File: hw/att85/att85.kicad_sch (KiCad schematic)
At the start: 45 parts, among them J101 Barrel_Jack_Switch, J102 Screw_Terminal_01x03, J103 AVR-ISP-6, J104 Conn_01x02, J105 Conn_01x02, Q101 BC817, SW101 SW_Push, SW102 SW_Push, SW103 SW_Push, SW104 SW_Push, SW105 SW_Push, SW106 SW_Push, U101 ATtiny85-20P, U102 MT3608-MODULE, U105 74AHC1G125

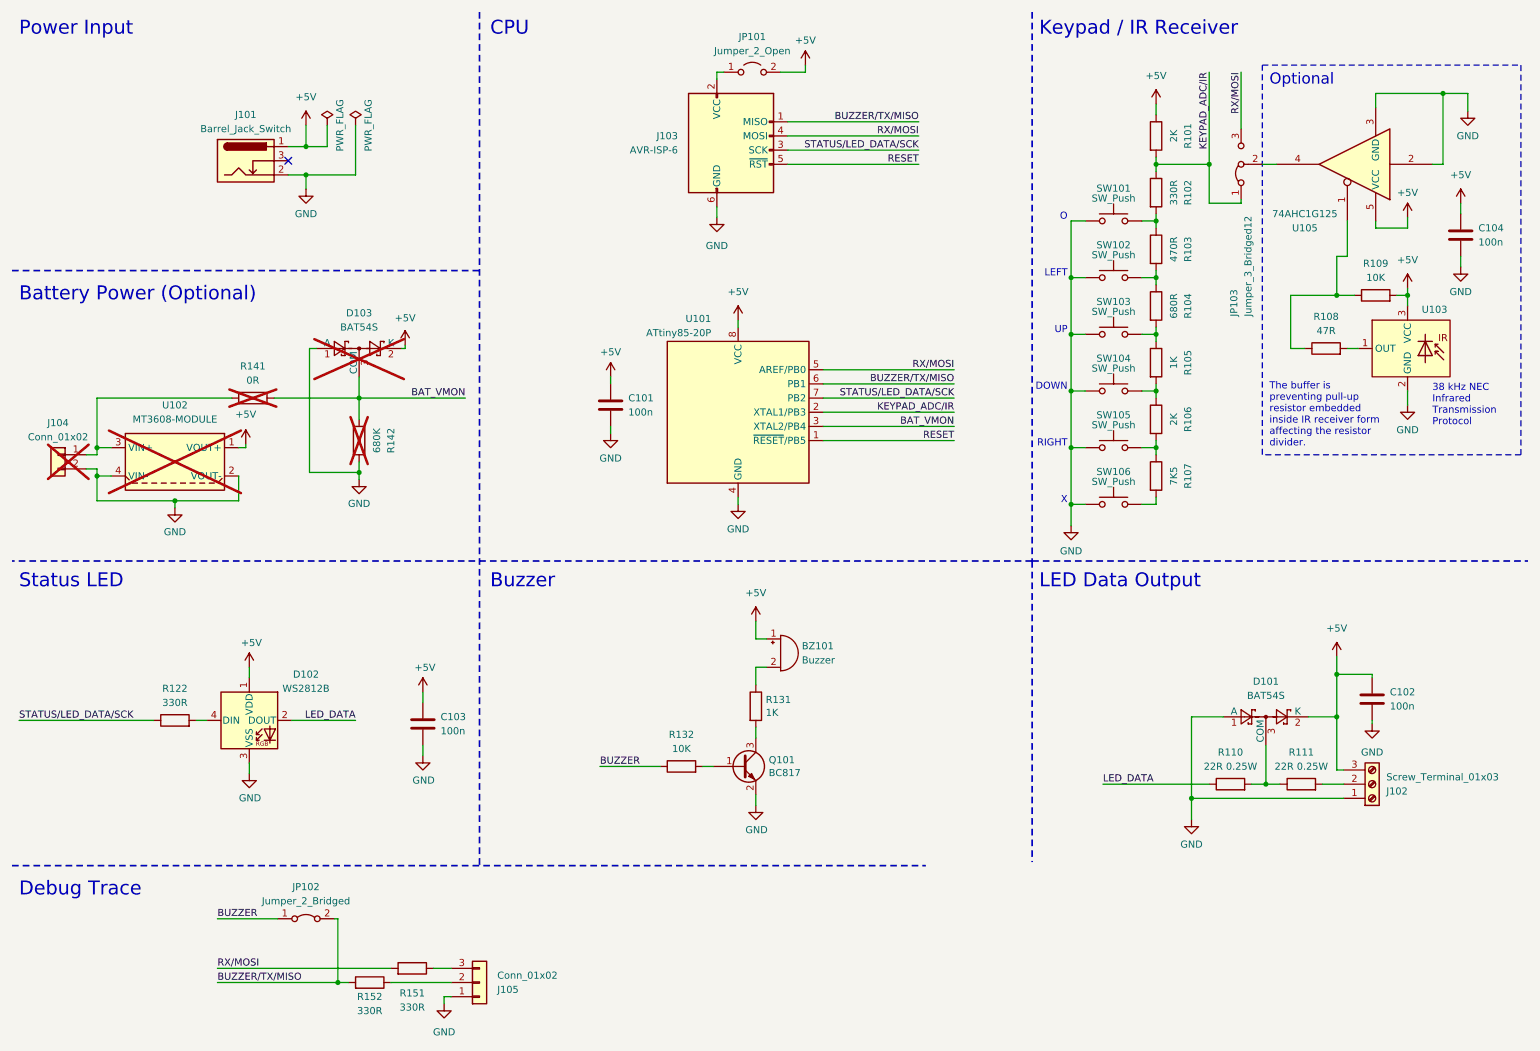
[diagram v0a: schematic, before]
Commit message: feat(hw): remove unused components, wire IR to separate uC pin
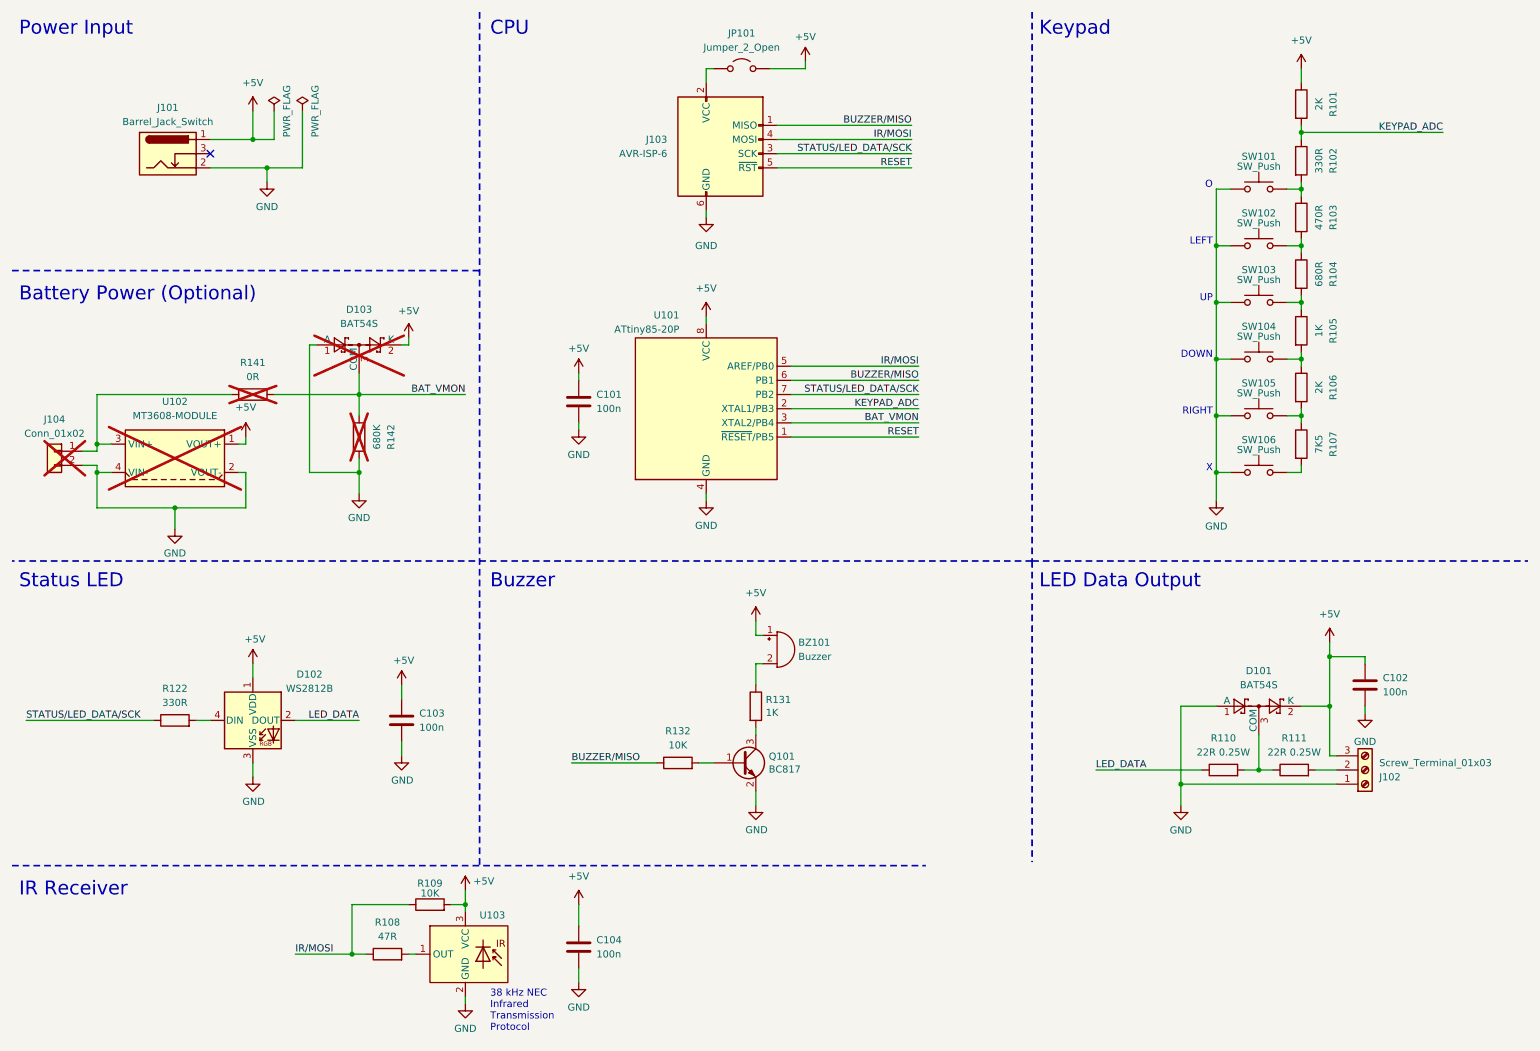
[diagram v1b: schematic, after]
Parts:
- removed J105: Conn_01x02, Connector_PinHeader_2.54mm:PinHeader_1x03_P2.54mm_Vertical, symbol Connector_Generic:Conn_01x03
- removed JP102: Jumper_2_Bridged, Jumper:SolderJumper-2_P1.3mm_Bridged_RoundedPad1.0x1.5mm, symbol Jumper:Jumper_2_Bridged
- removed JP103: Jumper_3_Bridged12, Jumper:SolderJumper-3_P1.3mm_Bridged12_RoundedPad1.0x1.5mm, symbol Jumper:Jumper_3_Bridged12
- removed R151, R152: 330R, Resistor_SMD:R_0805_2012Metric_Pad1.20x1.40mm_HandSolder, symbol Device:R
- removed U105: 74AHC1G125, Package_TO_SOT_SMD:SOT-23-5_HandSoldering, symbol 74xGxx:74AHC1G125
- U101: footprint Package_DIP:DIP-8_W7.62mm_Socket -> Package_DIP:DIP-8_W7.62mm
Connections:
- net BUZZER/TX/MISO is gone; now on net BUZZER/MISO: J103.1 (MISO), U101.6 (PB1)
- net RX/MOSI is gone; now on net IR/MOSI: J103.4 (MOSI), U101.5 (AREF/PB0)
- net IR/MOSI: now reaches R108.1, R109.1
- net BUZZER renamed BUZZER/MISO
- net KEYPAD_ADC/IR renamed KEYPAD_ADC
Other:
- note added: "IR Receiver"
- note added: "Keypad"
- note removed: "Debug Trace"
- note removed: "Keypad / IR Receiver"
- note removed: "Optional"
- note removed: "The buffer is preventing pull-up resistor embedded inside IR receiver form affecting the resistor divider."
- moved on the sheet: BZ101, C101, C102, C103, C104, D101, D102, D103, J101, J102, J103, J104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

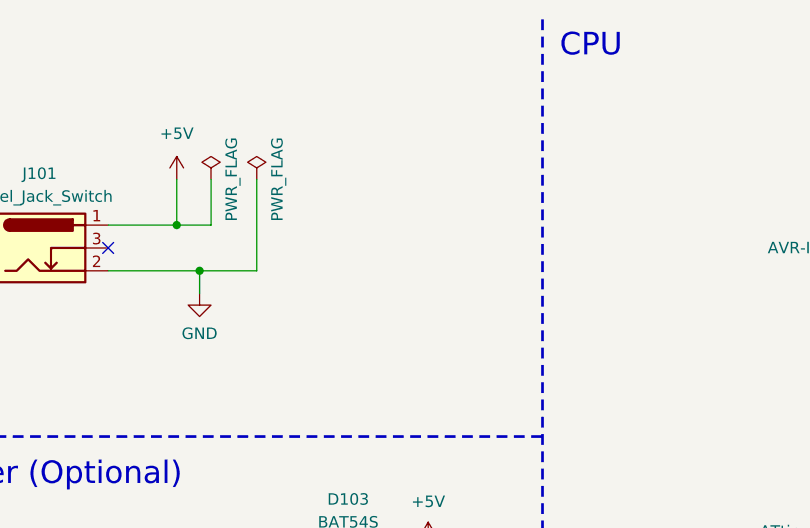
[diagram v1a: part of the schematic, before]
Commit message: feat(hw): improve layout and add a mounting hole
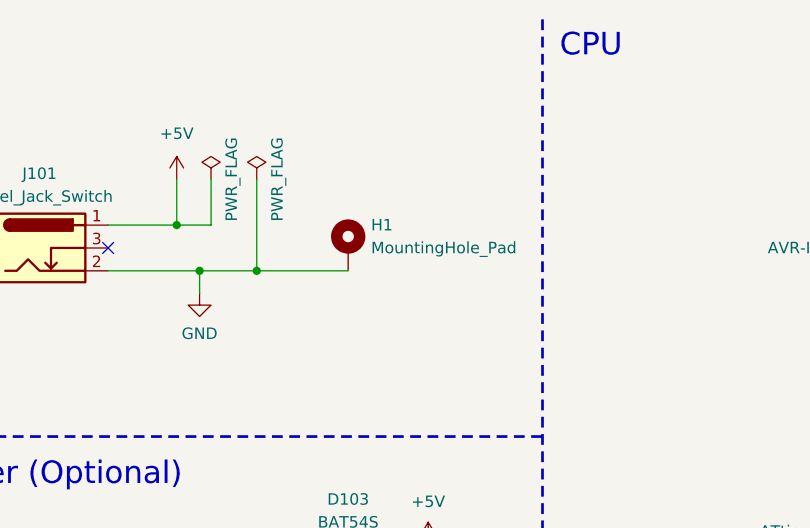
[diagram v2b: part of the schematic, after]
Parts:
- added H1: MountingHole_Pad, MountingHole:MountingHole_2.5mm_Pad_TopBottom, symbol Mechanical:MountingHole_Pad
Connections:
- net GND: now also H1.1
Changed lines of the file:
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@@
 	)
 	(junction
+		(at 64.77 40.64)
+		(diameter 0)
+		(color 0 0 0 0)
+	)
+	(junction
 		(at 243.84 74.93)
 		(diameter 0)
@@
 	(wire
 		(pts
+			(xy 64.77 40.64) (xy 74.93 40.64)
+		)
+		(stroke
+			(width 0)
+			(type default)
+		)
+	)
+	(wire
+		(pts
 			(xy 138.43 22.86) (xy 137.16 22.86)
 		)
@@
 					(unit 1)
 				)
+			)
+		)
+	)
+	(symbol
+		(lib_id "Mechanical:MountingHole_Pad")
+		(at 74.93 38.1 0)
+		(unit 1)
+		(exclude_from_sim yes)
+		(in_bom no)
+		(on_board yes)
+		(dnp no)
+		(fields_autoplaced yes)
+		(property "Reference" "H1"
+			(at 77.47 35.5599 0)
+			(effects
+				(font
+					(size 1.27 1.27)
+				)
+				(justify left)
+			)
+		)
+		(property "Value" "MountingHole_Pad"
+			(at 77.47 38.0999 0)
+			(effects
+				(font
+					(size 1.27 1.27)
+				)
+				(justify left)
+			)
+		)
+		(property "Footprint" "MountingHole:MountingHole_2.5mm_Pad_TopBottom"
+			(at 74.93 38.1 0)
+			(effects
+				(font
+					(size 1.27 1.27)
+				)
+				(hide yes)
+			)
+		)
+		(property "Datasheet" "~"
+			(at 74.93 38.1 0)
+			(effects
+				(font
+					(size 1.27 1.27)
+				)
+				(hide yes)
+			)
+		)
+		(property "Description" "Mounting Hole with connection"
+			(at 74.93 38.1 0)
+			(effects
+				(font
+					(size 1.27 1.27)
+				)
+				(hide yes)
+			)
+		)
+		(pin "1"
+		)
+		(instances
+			(project "att85"
+				(path "/fc4ba96f-a9f8-4f1a-a9c5-2b16679a6770"
+					(reference "H1")
+					(unit 1)
+				)

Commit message: fix(hw): minor improvements
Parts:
- added C105: 10u, Capacitor_SMD:C_1206_3216Metric_Pad1.33x1.80mm_HandSolder, symbol Device:C
- R109: value 10K -> 20K; now not fitted
- U103: value ~ -> VS1838B
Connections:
- net +5V: now also C105.1
- net GND: now also C105.2
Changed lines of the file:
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@@
 	)
 	(junction
+		(at 114.3 186.69)
+		(diameter 0)
+		(color 0 0 0 0)
+	)
+	(junction
 		(at 64.77 40.64)
 		(diameter 0)
@@
 	)
 	(junction
+		(at 114.3 173.99)
+		(diameter 0)
+		(color 0 0 0 0)
+	)
+	(junction
 		(at 228.6 85.09)
 		(diameter 0)
@@
 	(wire
 		(pts
+			(xy 114.3 186.69) (xy 114.3 184.15)
+		)
+		(stroke
+			(width 0)
+			(type default)
+		)
+	)
+	(wire
+		(pts
 			(xy 233.68 148.59) (xy 236.22 148.59)
 		)
@@
 	(wire
 		(pts
-			(xy 114.3 172.72) (xy 114.3 176.53)
+			(xy 114.3 172.72) (xy 114.3 173.99)
 		)
 		(stroke
@@
 	(wire
 		(pts
+			(xy 127 173.99) (xy 127 176.53)
+		)
+		(stroke
+			(width 0)
+			(type default)
+		)
+	)
+	(wire
+		(pts
 			(xy 83.82 71.12) (xy 83.82 72.39)
 		)
@@
 	(wire
 		(pts
-			(xy 114.3 186.69) (xy 114.3 184.15)
+			(xy 114.3 173.99) (xy 114.3 176.53)
+		)
+		(stroke
+			(width 0)
+			(type default)
+		)
+	)
+	(wire
+		(pts
+			(xy 114.3 187.96) (xy 114.3 186.69)
 		)
 		(stroke
@@
 	(wire
 		(pts
+			(xy 114.3 173.99) (xy 127 173.99)
+		)
+		(stroke
+			(width 0)
+			(type default)
+		)
+	)
+	(wire
+		(pts
 			(xy 255.27 138.43) (xy 255.27 137.16)
 		)
@@
 	(wire
 		(pts
+			(xy 114.3 186.69) (xy 127 186.69)
+		)
+		(stroke
+			(width 0)
+			(type default)
+		)
+	)
+	(wire
+		(pts
 			(xy 93.98 170.18) (xy 93.98 172.72)
 		)
@@
 	(wire
 		(pts
+			(xy 127 186.69) (xy 127 184.15)
+		)
+		(stroke
+			(width 0)
+			(type default)
+		)
+	)
+	(wire
+		(pts
 			(xy 73.66 172.72) (xy 73.66 181.61)
 		)
@@
 	(symbol
 		(lib_id "power:GND")
-		(at 114.3 186.69 0)
+		(at 114.3 187.96 0)
 		(unit 1)
 		(exclude_from_sim no)
@@
 		(fields_autoplaced yes)
 		(property "Reference" "#PWR0130"
-			(at 114.3 193.04 0)
+			(at 114.3 194.31 0)
 			(effects
 				(font
@@
 		)
 		(property "Value" "GND"
-			(at 114.3 191.135 0)
+			(at 114.3 192.405 0)
 			(effects
 				(font
@@
 		)
 		(property "Footprint" ""
-			(at 114.3 186.69 0)
+			(at 114.3 187.96 0)
 			(effects
 				(font
@@
 		)
 		(property "Datasheet" ""
-			(at 114.3 186.69 0)
+			(at 114.3 187.96 0)
 			(effects
 				(font
@@
 		)
 		(property "Description" "Power symbol creates a global label with name \"GND\" , ground"
-			(at 114.3 186.69 0)
+			(at 114.3 187.96 0)
 			(effects
 				(font
@@
 	)
 	(symbol
+		(lib_id "Device:C")
+		(at 127 180.34 0)
+		(unit 1)
+		(exclude_from_sim no)
+		(in_bom yes)
+		(on_board yes)
+		(dnp no)
+		(fields_autoplaced yes)
+		(property "Reference" "C105"
+			(at 130.175 179.07 0)
+			(effects
+				(font
+					(size 1.27 1.27)
+				)
+				(justify left)
+			)
+		)
+		(property "Value" "10u"
+			(at 130.175 181.61 0)
+			(effects
+				(font
+					(size 1.27 1.27)
+				)
+				(justify left)
+			)
+		)
+		(property "Footprint" "Capacitor_SMD:C_1206_3216Metric_Pad1.33x1.80mm_HandSolder"
+			(at 127.9652 184.15 0)
+			(effects
+				(font
+					(size 1.27 1.27)
+				)
+				(hide yes)
+			)
+		)
+		(property "Datasheet" "~"
+			(at 127 180.34 0)
+			(effects
+				(font
+					(size 1.27 1.27)
+				)
+				(hide yes)
+			)
+		)
+		(property "Description" "Unpolarized capacitor"
+			(at 127 180.34 0)
+			(effects
+				(font
+					(size 1.27 1.27)
+				)
+				(hide yes)
+			)
+		)
+		(pin "2"
+		)
+		(pin "1"
+		)
+		(instances
+			(project "att85"
+				(path "/fc4ba96f-a9f8-4f1a-a9c5-2b16679a6770"
+					(reference "C105")
+					(unit 1)
+				)
+			)
+		)
+	)
+	(symbol
 		(lib_id "Device:R")
 		(at 87.63 172.72 90)
@@
 		(in_bom yes)
 		(on_board yes)
-		(dnp no)
+		(dnp yes)
 		(property "Reference" "R109"
 			(at 87.63 168.91 90)
@@
 			)
 		)
-		(property "Value" "10K"
+		(property "Value" "20K"
 			(at 87.63 170.688 90)
 			(effects
@@
 		(dnp no)
 		(property "Reference" "U103"
-			(at 96.52 174.625 0)
+			(at 96.266 173.228 0)
 			(effects
 				(font
@@
 			)
 		)
-		(property "Value" "~"
-			(at 92.71 181.61 0)
+		(property "Value" "VS1838B"
+			(at 100.584 175.26 0)
 			(effects
 				(font

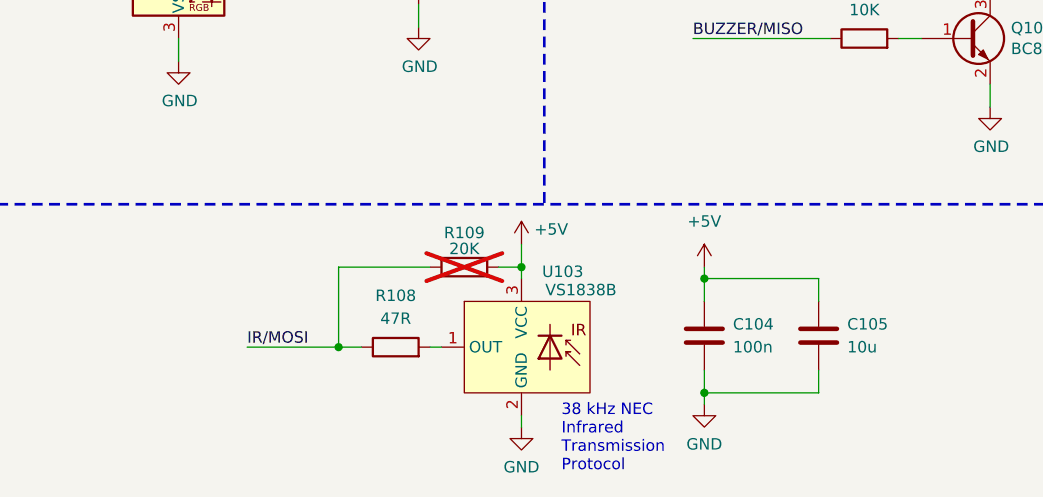
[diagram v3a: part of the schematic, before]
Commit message: fix(hw): move IR receiver resistor according the datasheet
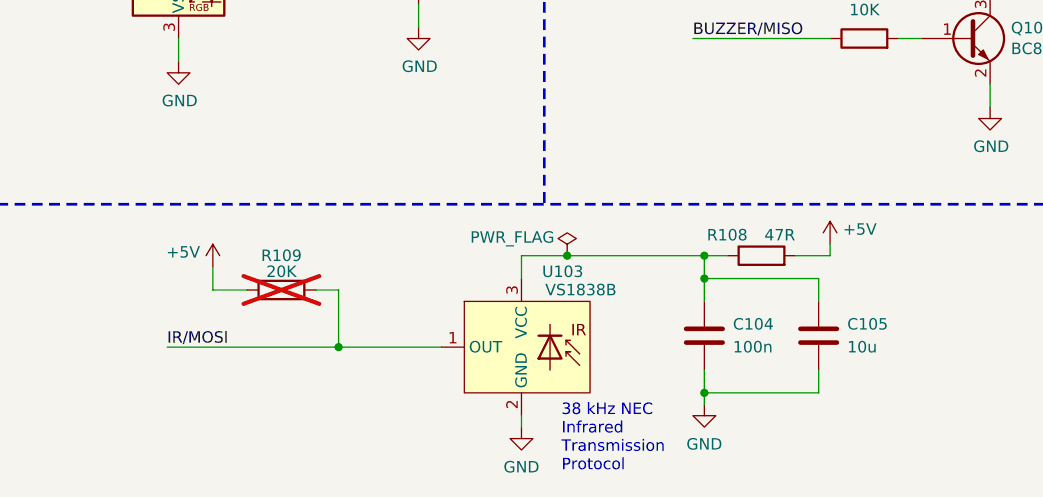
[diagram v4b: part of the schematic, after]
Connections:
- net +5V: now also R108.2; no longer C104.1, C105.1, U103.3 (VCC)
- net IR/MOSI: now also U103.1 (OUT); no longer R108.1
- new net: C104.1, C105.1, R108.1, U103.3 (VCC)
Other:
- moved on the sheet: R108, R109

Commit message: chore(hw): add STM32 CPU
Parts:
- removed C101: 100n, Capacitor_SMD:C_0805_2012Metric_Pad1.18x1.45mm_HandSolder, symbol Device:C
- removed J103: AVR-ISP-6, Connector_IDC:IDC-Header_2x03_P2.54mm_Vertical, symbol Connector:AVR-ISP-6
- removed JP101: Jumper_2_Open, Connector_PinHeader_2.54mm:PinHeader_1x02_P2.54mm_Vertical, symbol Jumper:Jumper_2_Open
- removed U101: ATtiny85-20P, Package_DIP:DIP-8_W7.62mm, symbol MCU_Microchip_ATtiny:ATtiny85-20P
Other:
- added sheet CPU (cpu.kicad_sch)
